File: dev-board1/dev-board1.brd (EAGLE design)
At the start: 100 x 80 mm, 156 parts, among them IC1 MSP432E401, IC10 CC3120MOD, IC2 MT48LC16M16A2, IC3 SIM800C, IC5 TPD3E001DRL, IC6 TPD3E001DRL, IC7 TPD3E001DRL, IC8 BQ25601, IC9 TPS62082, J1 MAGJACK-RJMG16XXX-8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

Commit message: ready to start routing
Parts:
- added JP15: JOYSTICK_MINI_MULTICOM_NOSILK, TiLDA Mk4 Parts:JOYSTICK_MULTICOMP_NOSILK
- added R35, R36, R37, R38, R39, R41: 1k, passives-7351:R0603-N
- added R40, R42, R43, R44: 5.6k, passives-7351:R0603-N
- added TP10, TP11, TP12, TP13, TP9: TP, Testpoint:TP
- moved R14 221.2 mm to (71.9, 77.0)
- moved TP7 216.0 mm to (60.1, 53.0), turned to 90 degrees
- moved R16 212.8 mm to (74.6, 63.4), turned to 90 degrees
- moved TP6 207.4 mm to (8.13, 61.4), turned to 90 degrees
- moved TP8 207.2 mm to (94.9, 21.3), turned to 90 degrees
- moved TP5 202.8 mm to (8.33, 58.9), turned to 90 degrees
- moved R34 194.5 mm to (68.5, 41.5), flipped to the bottom, turned to 270 degrees
- moved LED5 189.0 mm to (67.1, 39.0), flipped to the bottom, turned to 270 degrees
- moved TP4 168.7 mm to (67.7, 2.24), turned to 90 degrees
- moved TP3 165.6 mm to (65.4, 2.24), turned to 90 degrees
- moved TP1 162.9 mm to (3.25, 28.2)
- moved TP2 162.5 mm to (63.2, 2.24), turned to 90 degrees
- moved C57 151.4 mm to (23.4, 32.9)
- moved S6 148.9 mm to (58.7, 9.55), flipped to the bottom
- moved C55 148.2 mm to (25.6, 35.0)
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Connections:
- new net GGGG: IC3.2, R41.1, R42.1
- new net N$82: IC3.42, R36.1
- new net N$91: IC3.1, R37.1
- new net N$92: IC3.23, R39.1, R40.1
- new net N$93: JP14.2, R39.2
- new net N$94: IC3.3, TP9.P$1
- new net N$95: IC3.4, TP10.P$1
- new net N$96: IC3.5, TP11.P$1
- new net N$97: IC3.7, TP12.P$1
- new net N$98: IC3.6, TP13.P$1
- new net NETLIGHT_: IC3.41, Q4.1, R29.2, R35.1, TP4.P$1
- net +3V3: now also R43.1, R44.1
- net BQ_SCL: now also R43.2
- net BQ_SDA: now also R44.2
- net GND: now also R40.2, R42.2
- net N$72: now also IC3.22, R38.1; no longer IC3.23, JP14.2
- net N$77: now also R38.2; no longer IC3.22
- net NETLIGHT: now also R35.2; no longer IC3.41, Q4.1, R29.2, TP4.P$1
- net SIM_RX: now also R41.2; no longer IC3.2
- net SIM_STATUS: now also R36.2; no longer IC3.42
- net SIM_TX: now also R37.2; no longer IC3.1

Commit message: load of routing
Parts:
- moved R2 77.0 mm to (70.0, 75.4)
- moved C9 64.6 mm to (68.4, 75.4), turned to 90 degrees
- moved R4 64.1 mm to (66.8, 75.4), turned to 90 degrees
- moved S1 64.0 mm to (72.3, 74.0), flipped to the bottom
- moved S2 63.8 mm to (65.8, 74.0), flipped to the bottom
- moved R35 54.3 mm to (42.7, 49.8), turned to 0 degrees
- moved Q2 38.8 mm to (65.8, 32.3)
- moved C23 19.5 mm to (93.1, 71.5), flipped to the bottom, turned to 180 degrees
- moved R9 19.2 mm to (93.1, 69.9), flipped to the bottom
- moved C31 15.8 mm to (60.3, 8.08), turned to 90 degrees
- moved C16 10.8 mm to (94.8, 38.6)
- moved C32 9.76 mm to (56.8, 8.08), turned to 90 degrees
- moved C14 5.49 mm to (88.3, 55.8)
- moved C15 5.29 mm to (75.3, 53.1)
- moved C19 5.28 mm to (97.2, 55.6)
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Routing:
- net GND: track 298.7 -> 374.8 mm, vias 28 -> 42
- net CC_RST: track 0.00 -> 65.1 mm
- net S1: track 0.00 -> 55.7 mm, vias 0 -> 2
- net S2: track 0.00 -> 53.5 mm, vias 0 -> 2
- net CC_TX: track 0.00 -> 51.2 mm, vias 0 -> 3
- net CC_RX: track 0.00 -> 48.4 mm, vias 0 -> 2
- net S3: track 0.00 -> 47.2 mm
- net +3V3: track 54.3 -> 94.0 mm, vias 0 -> 10
- net ETHLED0: track 0.00 -> 34.8 mm, vias 0 -> 2
- net S30: track 0.00 -> 31.6 mm
- net S0: track 19.3 -> 49.6 mm, vias 0 -> 2
- net S31: track 17.1 -> 45.9 mm, vias 0 -> 4
- net CC_IRQ: track 0.00 -> 27.9 mm, vias 0 -> 2
- net S9: track 13.6 -> 39.5 mm, vias 0 -> 4
- net LCD_TEAR: track 0.00 -> 25.9 mm
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
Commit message: getting closer...
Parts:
- moved S3 52.6 mm to (74.2, 13.0)
- moved JP4 42.0 mm to (2.24, 43.3)
- moved R31 41.0 mm to (4.27, 44.3)
- moved JP14 35.0 mm to (29.7, 46.1), turned to 90 degrees
- moved JP2 34.3 mm to (4.47, 3.45), turned to 180 degrees
- moved C48 33.3 mm to (2.64, 75.6), turned to 180 degrees
- moved C28 32.5 mm to (25.4, 36.0), turned to 180 degrees
- moved TP6 31.4 mm to (23.8, 34.1)
- moved C27 31.0 mm to (19.3, 36.0), turned to 180 degrees
- moved C30 30.3 mm to (25.4, 37.6), turned to 180 degrees
- moved JP8 29.9 mm to (17.1, 25.4)
- moved C49 29.8 mm to (2.64, 73.8), turned to 180 degrees
- moved R30 29.6 mm to (13.2, 36.4), turned to 180 degrees
- moved TP5 28.0 mm to (21.3, 34.1)
- moved C51 28.0 mm to (3.66, 71.1), turned to 0 degrees
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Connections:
- net N$66: now also IC10.15, JP12.4; no longer IC10.14, JP12.2
- net N$69: now also IC10.14; no longer IC10.15
- net N$70: now also JP12.5; no longer JP12.4
- net N$71: now also JP12.2; no longer JP12.5
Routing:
- net +3V3: track 94.0 -> 201.1 mm, vias 10 -> 13
- net BQ_SCL: track 0.00 -> 77.2 mm, vias 0 -> 2
- net BQ_INT: track 0.00 -> 73.6 mm, vias 0 -> 5
- net BQ_SDA: track 0.00 -> 73.5 mm, vias 0 -> 3
- net VBAT_SWITCHED: track 13.4 -> 82.6 mm
- net GND: track 374.8 -> 422.8 mm, vias 42 -> 65
- net NETLIGHT_: track 0.00 -> 44.2 mm
- net N$82: track 0.00 -> 40.0 mm, vias 0 -> 2
- net N$38: track 0.00 -> 39.5 mm, vias 0 -> 2
- net N$53: track 0.00 -> 38.7 mm, vias 0 -> 2
- net N$42: track 0.00 -> 38.6 mm, vias 0 -> 2
- net N$91: track 0.00 -> 37.1 mm, vias 0 -> 2
- net GGGG: track 0.00 -> 34.2 mm, vias 0 -> 2
- net NRST: track 52.4 -> 19.0 mm, vias 5 -> 2
- net SWO: track 33.6 -> 1.05 mm
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
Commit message: load of routing again
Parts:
- moved TP3 63.7 mm to (35.2, 58.3)
- moved TP4 59.2 mm to (27.0, 45.3), flipped to the bottom
- moved S3 44.9 mm to (29.3, 12.6), turned to 180 degrees
- moved JP15 12.4 mm to (50.0, 48.4), turned to 45 degrees
- moved TP8 10.6 mm to (92.7, 31.7)
- moved TP2 7.40 mm to (56.1, 4.27)
- moved TP9 5.82 mm to (9.35, 55.1)
- moved L2 5.31 mm to (54.2, 68.9), turned to 0 degrees
- moved TP1 3.41 mm to (6.50, 23.2)
- moved J4 3.15 mm to (39.4, 66.4)
- moved R4 2.80 mm to (65.9, 78.1), turned to 0 degrees
- moved Q3 2.73 mm to (30.9, 41.2), turned to 180 degrees
- moved C9 2.71 mm to (65.9, 76.5), turned to 0 degrees
- moved TP13 2.64 mm to (14.4, 55.1)
- moved R32 2.09 mm to (53.6, 5.79)
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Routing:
- net +3V3: track 201.1 -> 488.8 mm, vias 13 -> 26
- net NRST: track 19.0 -> 88.1 mm, vias 2 -> 5
- net N$76: track 0.00 -> 52.4 mm, vias 0 -> 1
- net USB_VBUS: track 40.1 -> 86.6 mm, vias 2 -> 4
- net V_UNREG: track 18.4 -> 61.8 mm, vias 0 -> 4
- net LCD_CLK: track 14.9 -> 54.1 mm, vias 2 -> 4
- net N$9: track 1.66 -> 39.9 mm, vias 0 -> 4
- net SWO: track 1.05 -> 33.6 mm, vias 0 -> 2
- net GND: track 422.8 -> 450.7 mm, vias 65 -> 138
- net N$53: track 38.7 -> 66.4 mm, vias 2 -> 4
- net SWCLK: track 12.8 -> 37.5 mm, vias 0 -> 3
- net N$74: track 7.34 -> 30.9 mm, vias 0 -> 2
- net PWR_KEY: track 0.00 -> 22.3 mm, vias 0 -> 2
- net LCD_TEAR: track 25.9 -> 47.8 mm, vias 0 -> 1
- net USB_ID: track 6.08 -> 27.7 mm, vias 0 -> 2
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- added copper zone on layer 1, net GND

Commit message: load of routing again again
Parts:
- moved C14 0.41 mm to (88.3, 55.4)
- moved C18 0.41 mm to (90.1, 55.4)
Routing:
- net S12: track 26.0 -> 87.8 mm, vias 0 -> 8
- net +3V3: track 488.8 -> 509.5 mm, vias 26 -> 27
- net S30: track 31.6 -> 50.4 mm, vias 0 -> 4
- net USB_VBUS: track 86.6 -> 100.5 mm
- net S10: track 37.3 -> 49.9 mm
- net S29: track 17.3 -> 27.5 mm, vias 0 -> 2
- net N$76: track 52.4 -> 62.5 mm, vias 1 -> 2
- net S0: track 49.6 -> 57.5 mm
- net ETHLED2: track 13.5 -> 7.79 mm
- net LCD_TEAR: track 47.8 -> 53.4 mm
- net S28: track 57.1 -> 62.6 mm, vias 1 -> 2
- net S7: track 50.0 -> 54.0 mm, vias 3 -> 4
- net GND: track 450.7 -> 454.7 mm, vias 138 -> 143
- net LCD_CLK: track 54.1 -> 50.2 mm
- net S15: track 67.5 -> 70.9 mm, vias 1 -> 2
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- added copper zone on layer 16, net GND

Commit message: load of routing again again again
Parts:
- moved R8 8.28 mm to (56.8, 67.5), turned to 90 degrees
- moved C15 1.48 mm to (75.0, 53.1), turned to 180 degrees
- moved L2 1.02 mm to (53.4, 69.5)
- moved JP15 0.81 mm to (50.0, 49.2)
- moved C7 0.61 mm to (52.1, 59.1)
- moved R32 0.61 mm to (53.0, 5.79)
- moved R31 0.51 mm to (3.96, 43.9)
- moved C1 0.41 mm to (67.2, 42.4)
- moved C4 0.20 mm to (66.2, 48.5)
- moved C38 0.16 mm to (7.52, 47.3)
- moved R13 0.11 mm to (7.52, 45.7)
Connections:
- new net JOYC: IC1.60, JP15.CTR
- new net JOYD: IC1.72, JP15.D
- new net JOYL: IC1.73, JP15.C
- new net JOYR: IC1.74, JP15.B
- new net JOYU: IC1.71, JP15.A
- net GND: now also JP15.COM
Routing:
- net +3V3: track 509.5 -> 545.2 mm, vias 27 -> 29
- net S29: track 27.5 -> 55.1 mm, vias 2 -> 6
- net NRST: track 88.1 -> 69.0 mm, vias 5 -> 6
- net N$16: track 9.33 -> 25.0 mm
- net JOYL: track 0.00 -> 14.8 mm, vias 0 -> 1
- net USB_ID: track 27.7 -> 13.4 mm, vias 2 -> 0
- net N$2: track 8.44 -> 22.4 mm, vias 0 -> 2
- net S11: track 27.1 -> 39.8 mm, vias 2 -> 5
- net JOYC: track 0.00 -> 12.2 mm, vias 0 -> 1
- net JOYR: track 0.00 -> 11.9 mm, vias 0 -> 1
- net GND: track 454.7 -> 443.2 mm, vias 143 -> 144
- net JOYU: track 0.00 -> 10.2 mm, vias 0 -> 1
- net S14: track 65.3 -> 59.3 mm, vias 0 -> 2
- net JOYD: track 0.00 -> 4.24 mm, vias 0 -> 1
- net N$17: track 9.60 -> 13.6 mm
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
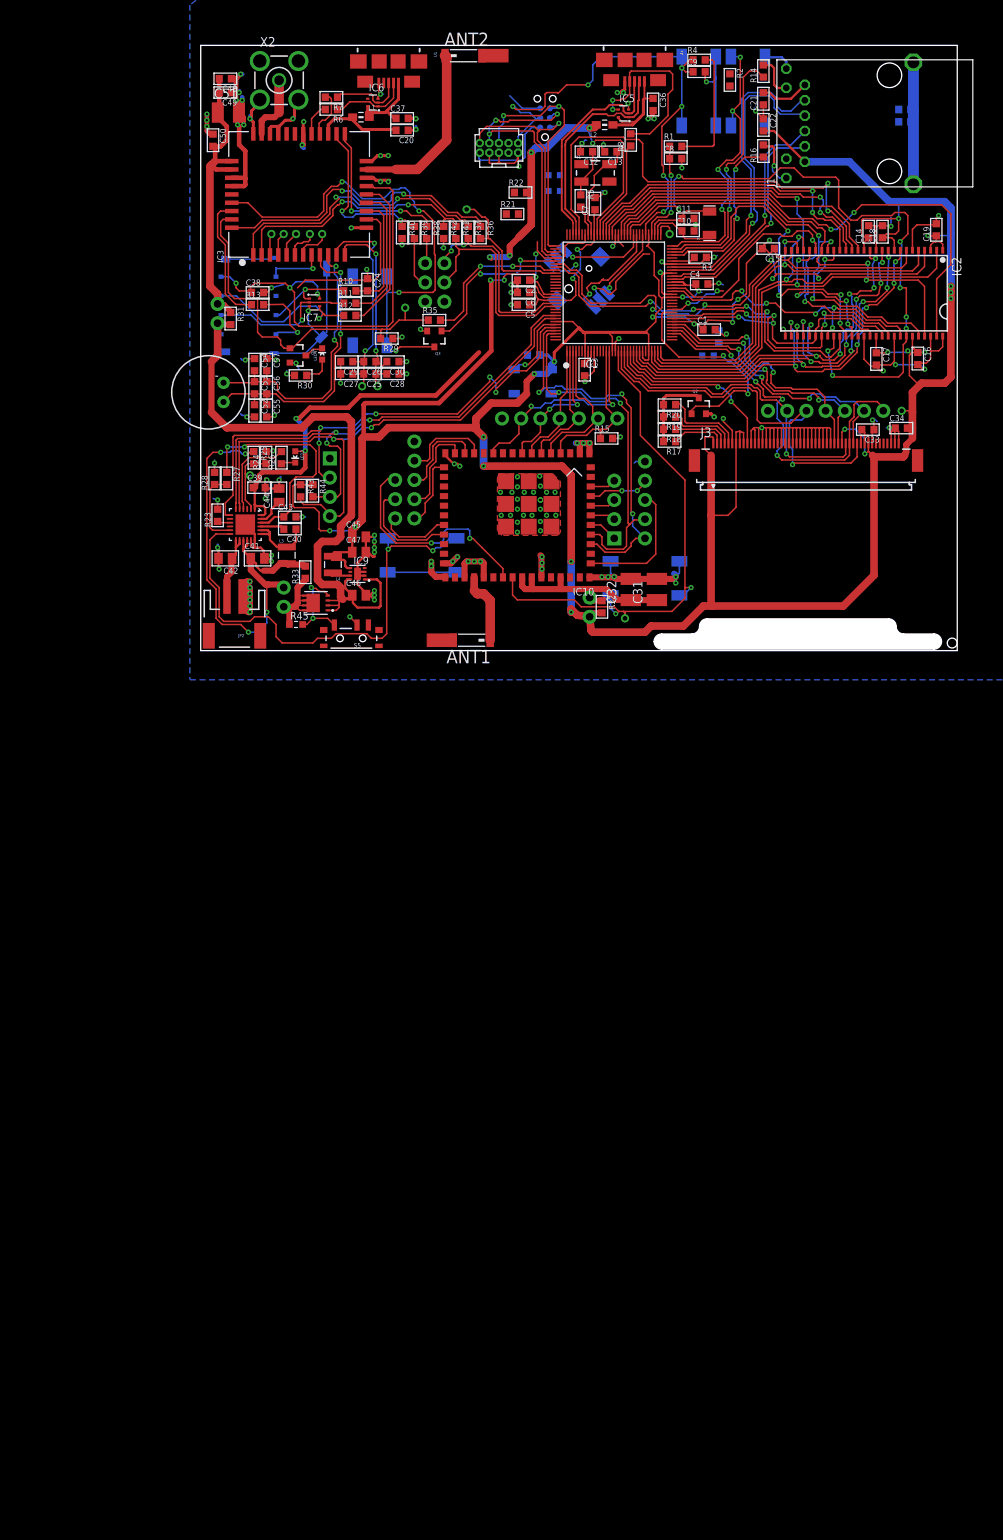
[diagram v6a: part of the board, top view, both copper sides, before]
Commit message: adding extra audio paths
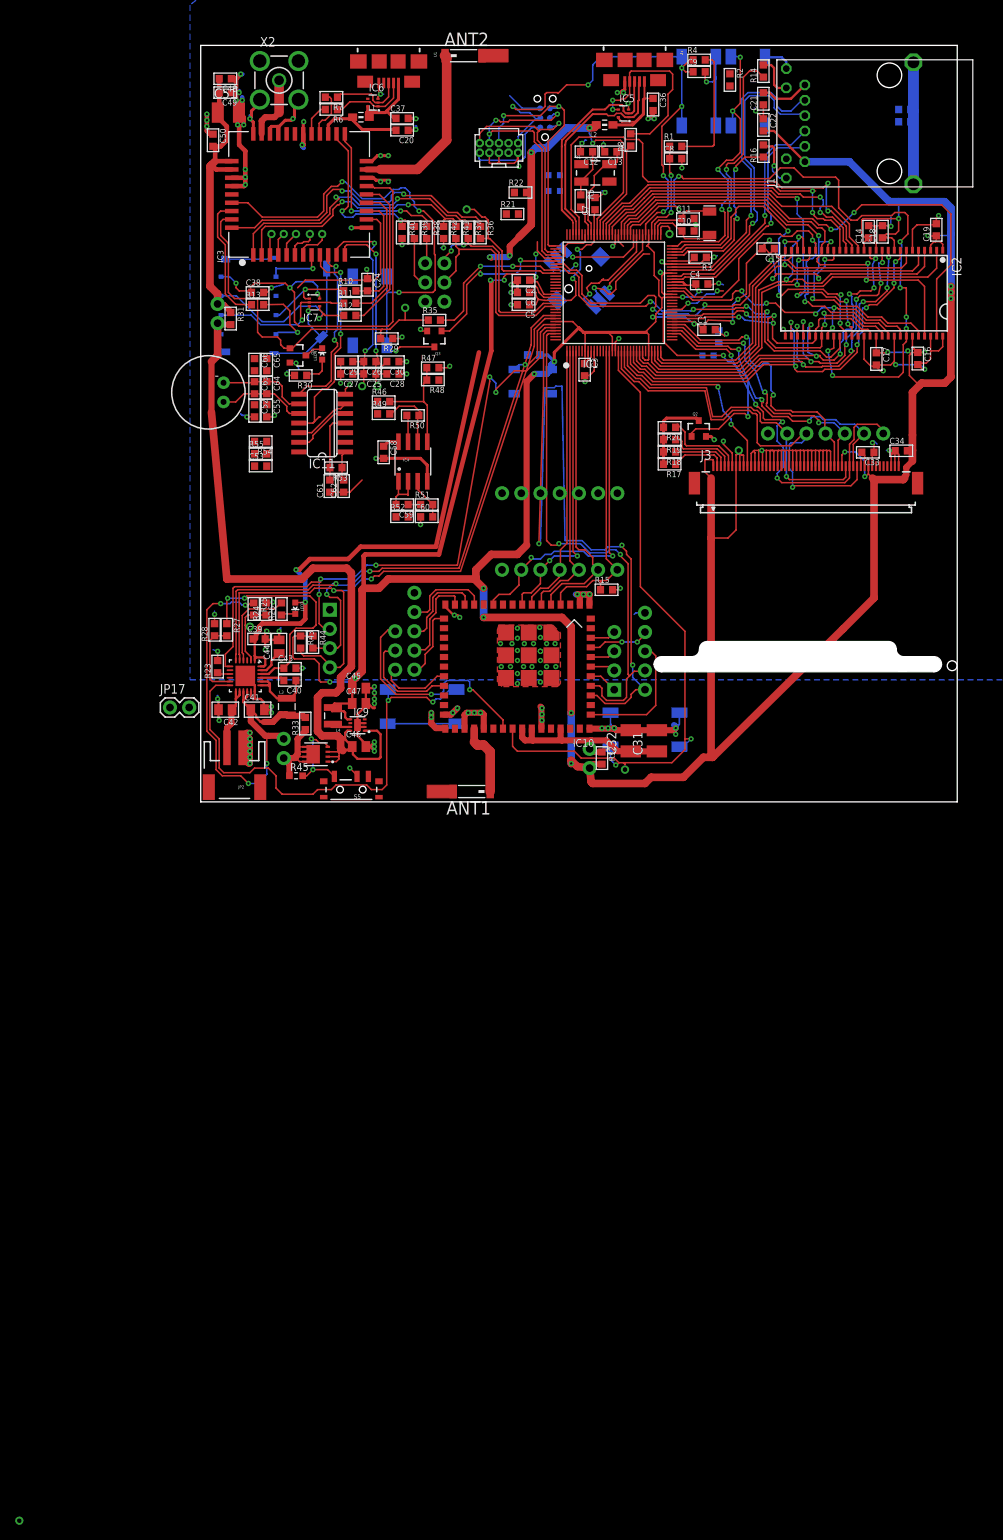
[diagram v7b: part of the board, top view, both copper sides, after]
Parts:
- added C58, C61: 100n, passives-7351:C0603-N
- added C59: 2.2n, passives-7351:C0603-N
- added C60: 1n, passives-7351:C0603-N
- added C62: dnp, passives-7351:C0603-N
- added C63: 33p, passives-7351:C0603-N
- added IC11: 4066D, 40xx:SO14
- added IC4: OPAMP-DUALU, SparkFun-AnalogIC:SO08
- added JP16: (no value), TiLDA Mk4 Parts:1X07
- added JP17: (no value), TiLDA Mk4 Parts:1X02
- added R46, R49, R50, R53, R54, R55: 10k, passives-7351:R0603-N
- added R47, R48: 22k, passives-7351:R0603-N
- added R51: 14.7k, passives-7351:R0603-N
- added R52: 7.87k, passives-7351:R0603-N
- added TP15: TP, Testpoint:TP
- C53: value 10p -> 100n
- C64, C65: value 33p -> 10p
- C66: value 10p -> 33p
- moved TP8 22.2 mm to (71.1, 26.5)
- moved ANT1 20.0 mm to (35.8, -18.6)
- moved C31 20.0 mm to (60.3, -11.9)
- moved C32 20.0 mm to (56.8, -11.9)
- moved C39 20.0 mm to (7.72, 1.54)
- moved C40 20.0 mm to (11.8, -3.95)
- moved C41 20.0 mm to (7.52, -7.81)
- moved C42 20.0 mm to (3.25, -7.81)
- moved C43 20.0 mm to (11.8, -2.32)
- moved C44 20.0 mm to (10.4, 0.52)
- moved C45 20.0 mm to (20.9, -4.96)
- moved C46 20.0 mm to (20.9, -12.7)
- moved C47 20.0 mm to (20.9, -7.00)
- moved IC10 20.0 mm to (41.9, -2.12)
- moved IC8 20.0 mm to (5.89, -3.34)
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- renumbered C54 to C66, C56 to C64, C57 to C65
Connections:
- new net ADC: IC1.128, IC4.7, R50.2
- new net N$100: C59.1, R51.1, R52.2
- new net N$101: C61.2, IC11.4, R53.2
- new net N$102: C62.2, IC11.1, R53.1
- new net N$105: IC11.13, IC11.5, R55.2
- new net N$108: C52.1, C55.1, C63.2, C64.2, IC11.10, U$1.1
- new net N$81: C63.1, C64.1, C65.2, C66.2, IC11.9, U$1.2
- new net N$87: IC4.6, R49.2, R50.1
- new net N$89: IC11.12, IC11.6, R54.1
- new net N$90: C59.2, C61.1, C62.1, IC4.1, IC4.2, TP15.P$1
- new net N$99: C60.2, IC4.3, R51.2
- new net PWM: IC1.45, JP17.2, R52.1
- new net SSI3CLK: IC1.5, JP16.2
- new net SSI3DAT0: IC1.11, JP16.4
- new net SSI3DAT1: IC1.27, JP16.5
- new net SSI3DAT2: IC1.46, JP16.6
- new net SSI3DAT3: IC1.119, JP16.7
- new net SSI3FSS: IC1.6, JP16.3
- net +3V3: now also C53.2, C58.1, IC11.14, IC4.8, R48.1, R54.2
- net GND: now also C53.1, C58.2, C60.1, IC11.7, IC4.4, JP16.1, JP17.1, R47.2, R55.1
- net N$37: now also IC4.5, R46.2, R47.1, R48.2; no longer IC1.45
- net N$38: now also IC11.11, IC11.3; no longer C52.1, C53.2, C55.1, C64.2, U$1.1
- net N$40: now also R49.1
- net N$41: now also R46.1
- net N$42: now also IC11.2, IC11.8; no longer C53.1, C64.1, C65.2, C66.2, U$1.2
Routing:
- net +3V3: track 545.2 -> 611.7 mm
- net CC_TX: track 51.0 -> 110.3 mm
- net CC_MOSI: track 17.1 -> 37.1 mm
- net CC_IRQ: track 27.9 -> 47.9 mm
- net CC_RST: track 70.1 -> 90.1 mm
- net CC_CS: track 19.2 -> 39.2 mm
- net CC_MISO: track 16.0 -> 36.0 mm
- net CC_CLK: track 19.5 -> 39.5 mm
- net CC_HIB: track 21.1 -> 41.1 mm
- net CC_RX: track 47.6 -> 67.6 mm
- net VBAT_SWITCHED: track 84.2 -> 103.4 mm
- net BQ_INT: track 72.8 -> 91.4 mm
- net USB_VBUS: track 98.8 -> 117.1 mm
- net BQ_SDA: track 73.7 -> 91.3 mm
- net BQ_SCL: track 77.4 -> 94.9 mm
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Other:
- board size 100 x 80 mm -> 100 x 100 mm

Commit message: getting close
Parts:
- moved TP15 144.6 mm to (23.0, 21.7), flipped to the bottom
- moved JP17 37.0 mm to (24.8, 15.6), flipped to the bottom, turned to 180 degrees
- moved S6 24.3 mm to (83.0, -11.4), turned to 270 degrees
- moved JP4 19.1 mm to (2.44, 24.2)
- moved R31 18.5 mm to (4.17, 25.4)
- moved JP9 16.5 mm to (64.3, -10.6), turned to 180 degrees
- moved LED5 10.9 mm to (70.5, 49.4)
- moved JP10 9.71 mm to (64.3, -6.10), turned to 180 degrees
- moved R34 8.18 mm to (70.5, 49.4), flipped to the top, turned to 180 degrees
- moved R47 5.70 mm to (31.1, 31.7)
- moved LED2 5.31 mm to (44.8, 57.9), turned to 180 degrees
- moved R21 5.13 mm to (46.3, 57.9), turned to 270 degrees
- moved R52 3.80 mm to (30.3, 18.7), turned to 270 degrees
- moved R22 3.59 mm to (44.7, 57.9), turned to 270 degrees
- moved R51 2.91 mm to (27.0, 18.7), turned to 90 degrees
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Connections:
- removed net N$105: IC11.13, IC11.5, R55.2
- removed net N$89: IC11.12, IC11.6, R54.1
- new net MUX_A: IC1.108, IC11.12, IC11.6, R54.1
- new net MUX_B: IC1.109, IC11.13, IC11.5, R55.2
- net JOYC: now also IC1.107, IC1.118; no longer IC1.60
- net PWR_KEY: now also IC1.106; no longer IC1.102
- net SIM_STATUS: now also IC1.102; no longer IC1.106
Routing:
- net MUX_B: track 0.00 -> 51.2 mm
- net MUX_A: track 0.00 -> 50.6 mm
- net CC_RST: track 90.1 -> 133.9 mm, vias 2 -> 1
- net PWM: track 0.00 -> 42.9 mm, vias 0 -> 2
- net +3V3: track 611.7 -> 654.5 mm, vias 29 -> 33
- net CC_RX: track 67.6 -> 101.5 mm, vias 2 -> 4
- net SSI3DAT1: track 0.00 -> 32.6 mm, vias 0 -> 2
- net ADC: track 3.55 -> 35.0 mm, vias 0 -> 2
- net SSI3DAT2: track 0.00 -> 30.4 mm, vias 0 -> 2
- net SSI3DAT3: track 0.00 -> 30.3 mm, vias 0 -> 2
- net SSI3FSS: track 0.00 -> 24.7 mm
- net SSI3CLK: track 0.00 -> 24.6 mm
- net N$54: track 3.42 -> 24.9 mm
- net SSI3DAT0: track 0.00 -> 20.8 mm
- net CC_MISO: track 36.0 -> 56.8 mm
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- added copper zone on layer 16, net N$88
